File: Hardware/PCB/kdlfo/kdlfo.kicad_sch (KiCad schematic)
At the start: 51 parts, among them J1 Synth_power_2x5, J10 AudioJack2, J11 AudioJack2, J12 2 PIN MOLEX HEADER, J13 2 PIN MOLEX CONNECTOR, J2 2 PIN MOLEX HEADER, J3 2 PIN MOLEX HEADER, J4 AudioJack2, J5 2 PIN MOLEX HEADER, J6 2 PIN MOLEX CONNECTOR, J7 2 PIN MOLEX CONNECTOR, J8 2 PIN MOLEX CONNECTOR, J9 3 POSITION PIN HEADER, Q1 J201, Q2 J201, U1 TL074, U2 TL074

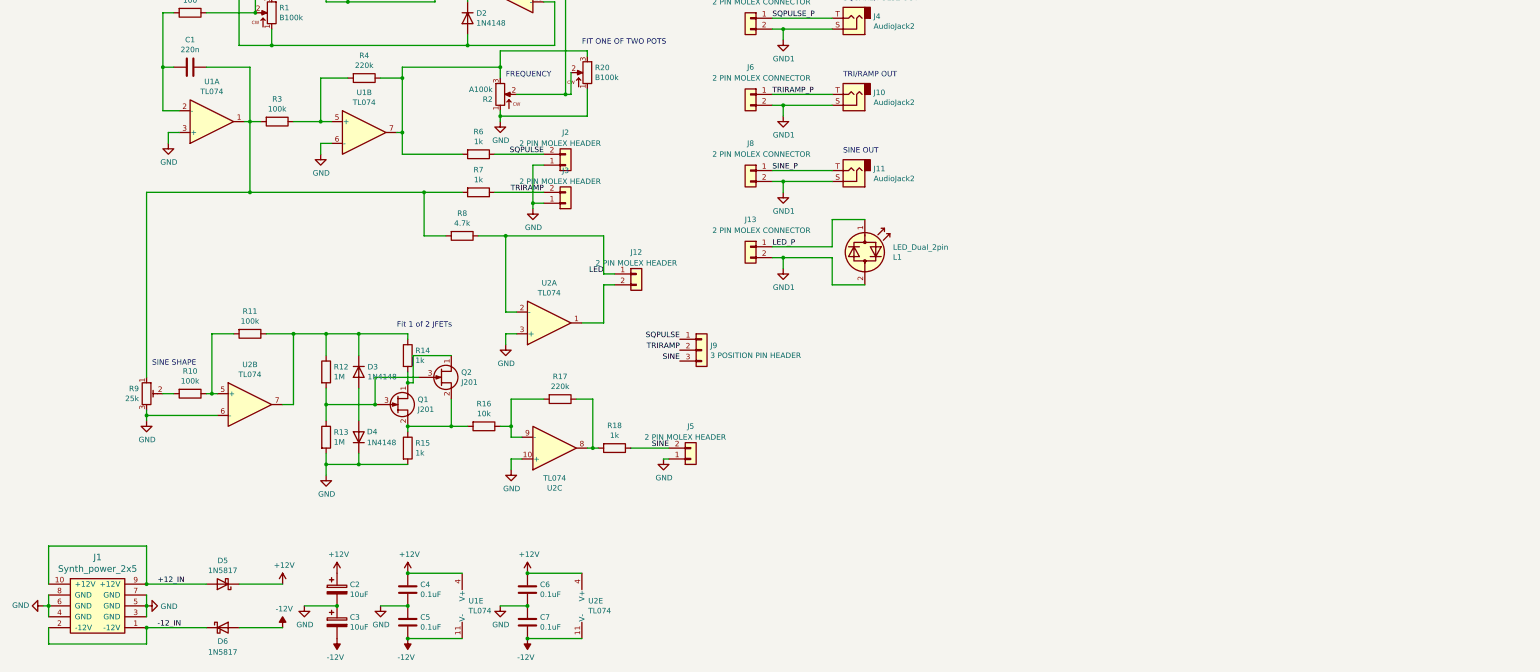
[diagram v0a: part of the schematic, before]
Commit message: Replace sine shaper, add divider on pulse output
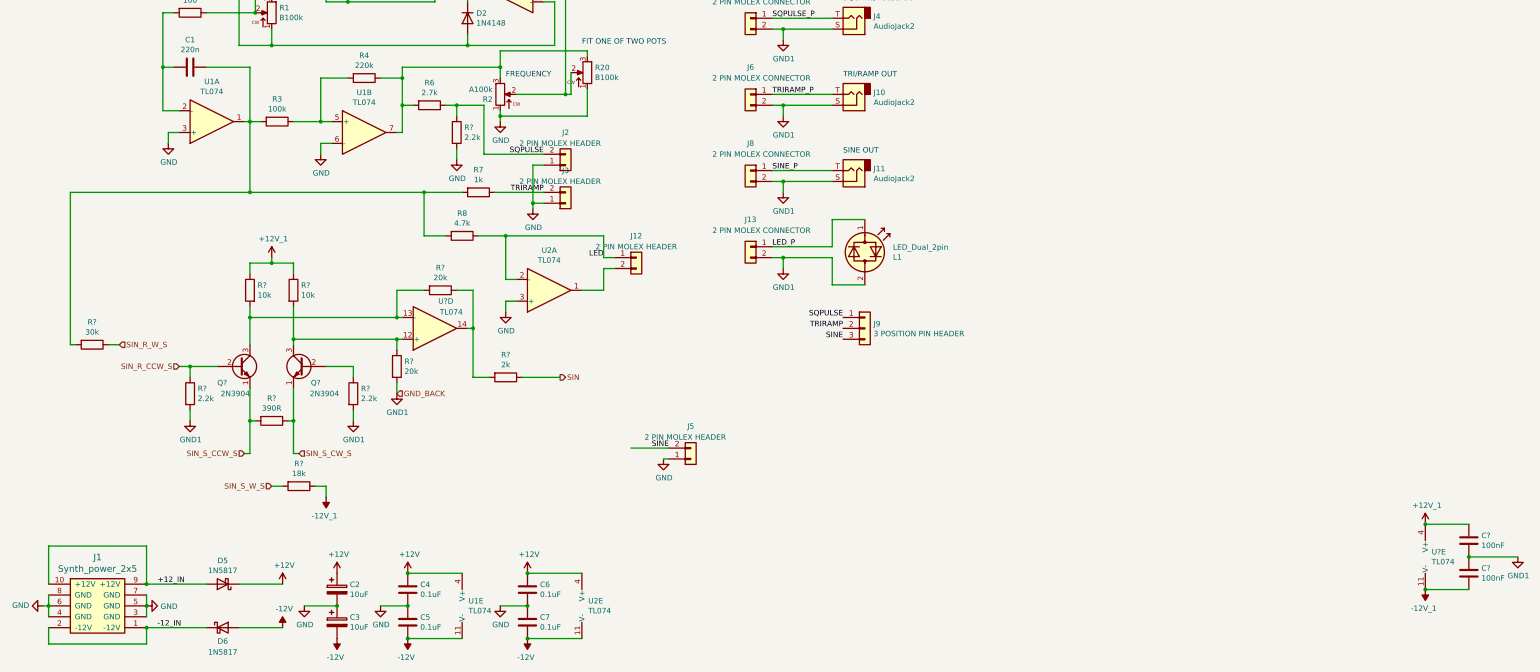
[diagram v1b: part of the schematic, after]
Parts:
- removed D3, D4: 1N4148, ao_tht:D_DO-35_SOD27_P7.62mm_Horizontal, symbol Diode:1N4148
- removed Q1: J201, ao_tht:TO-92_Inline_Wide, symbol Device:Q_NJFET_DSG
- removed Q2: J201, Package_TO_SOT_SMD:SOT-23, symbol Device:Q_NJFET_DSG
- removed R10, R11: 100k, ao_tht:R_Axial_DIN0207_L6.3mm_D2.5mm_P10.16mm_Horizontal, symbol Device:R
- removed R12, R13: 1M, ao_tht:R_Axial_DIN0207_L6.3mm_D2.5mm_P10.16mm_Horizontal, symbol Device:R
- removed R14, R15, R18: 1k, ao_tht:R_Axial_DIN0207_L6.3mm_D2.5mm_P10.16mm_Horizontal, symbol Device:R
- removed R16: 10k, ao_tht:R_Axial_DIN0207_L6.3mm_D2.5mm_P10.16mm_Horizontal, symbol Device:R
- removed R17: 220k, ao_tht:R_Axial_DIN0207_L6.3mm_D2.5mm_P10.16mm_Horizontal, symbol Device:R
- removed R9: 25k, ao_tht:Potentiometer_Bourns_3296W_Vertical, symbol Device:R_POT_TRIM
- removed unit 2 of U2
- removed unit 3 of U2
- added C? (x2): 100nF, ao_tht:C_Disc_D3.0mm_W1.6mm_P2.50mm, symbol ao_symbols:C
- added Q? (x2): 2N3904, ao_tht:TO-92_Inline_Wide, symbol ao_symbols:2N3904
- added R? (x2): 20k, ao_tht:R_Axial_DIN0207_L6.3mm_D2.5mm_P10.16mm_Horizontal, symbol ao_symbols:R
- added R? (x3): 2.2k, ao_tht:R_Axial_DIN0207_L6.3mm_D2.5mm_P10.16mm_Horizontal, symbol ao_symbols:R
- added R? (x2): 10k, ao_tht:R_Axial_DIN0207_L6.3mm_D2.5mm_P10.16mm_Horizontal, symbol ao_symbols:R
- added R?: 390R, ao_tht:R_Axial_DIN0207_L6.3mm_D2.5mm_P10.16mm_Horizontal, symbol ao_symbols:R
- added R?: 2k, ao_tht:R_Axial_DIN0207_L6.3mm_D2.5mm_P10.16mm_Horizontal, symbol ao_symbols:R
- added R?: 18k, ao_tht:R_Axial_DIN0207_L6.3mm_D2.5mm_P10.16mm_Horizontal, symbol ao_symbols:R
- added R?: 30k, ao_tht:R_Axial_DIN0207_L6.3mm_D2.5mm_P10.16mm_Horizontal, symbol ao_symbols:R
- added U? (x2): TL074, ao_tht:DIP-14_W7.62mm_Socket_LongPads, symbol Amplifier_Operational:TL074
- R6: value 1k -> 2.7k
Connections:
- net GND: now also R?.2
- net GND1: now also C?.1, C?.2, R?.2, R?.2, R?.2
- net SQPULSE: now also R?.1
- net at C1.1, R3.2, R7.2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: now also R?.2
- new net: R?.1, R?.2, U?.14
- new net: Q?.3 (C), R?.2, R?.2, U?.13 (-)
- new net: Q?.3 (C), R?.1, R?.2, U?.12 (+)
- new net: Q?.2 (B), R?.1
- new net +12V_1: C?.1, R?.1, R?.1, U?.4 (V+)
- new net -12V_1: C?.2, R?.1, U?.11 (V-)
- new net SIN: R?.1
- new net SIN_R_CCW_S: Q?.2 (B), R?.1
- new net SIN_R_W_S: R?.1
- new net SIN_S_CCW_S: Q?.1 (E), R?.2
- new net SIN_S_CW_S: Q?.1 (E), R?.1
- new net SIN_S_W_S: R?.2
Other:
- note removed: "Fit 1 of 2 JFETs"
- note removed: "SINE SHAPE"
- moved on the sheet: J12, J9, R6, U2A

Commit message: Better .gitignore; rm extraneous footprint library; misc revisions
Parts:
- removed J12, J2, J3, J5: 2 PIN MOLEX HEADER, ao_tht:Molex_KK-254_AE-6410-02A_1x02_P2.54mm_Vertical, symbol Connector_Generic:Conn_01x02
- removed J13, J6, J7, J8: 2 PIN MOLEX CONNECTOR, ao_tht:Molex_KK-254_AE-6410-02A_1x02_P2.54mm_Vertical, symbol Connector_Generic:Conn_01x02
- removed J9: 3 POSITION PIN HEADER, Connector_PinSocket_2.54mm:PinSocket_1x03_P2.54mm_Vertical, symbol Connector_Generic:Conn_01x03
- removed R19: B100k, ao_tht:Potentiometer_Alpha_RD901F-40-00D_Single_Vertical_CircularHoles, symbol ao_symbols:R_POT
- removed R2: A100k, Potentiometer_THT:Potentiometer_Piher_T-16H_Single_Horizontal, symbol ao_symbols:R_POT
- removed R?: 18k, ao_tht:R_Axial_DIN0207_L6.3mm_D2.5mm_P10.16mm_Horizontal, symbol ao_symbols:R
- added C1: 220n, ao_tht:C_Rect_L7.2mm_W2.5mm_P5.00mm_FKS2_FKP2_MKS2_MKP2, symbol Device:C
- added D1, D3: 1N4148, ao_tht:D_DO-35_SOD27_P7.62mm_Horizontal, symbol Diode:1N4148
- added D5: LED_Dual_2pin, ao_tht:LED_D5.0mm, symbol Device:LED_Dual_2pin
- added GRAF1: Holes, kdlfo:kdlfo_panel_holes, symbol ao_symbols:Graphic
- added J1, J3, J5, J7: 3_pin_Molex_header, ao_tht:Molex_KK-254_AE-6410-03A_1x03_P2.54mm_Vertical, symbol ao_symbols:3_pin_Molex_header
- added J11, J13, J9: AudioJack2, ao_tht:Jack_6.35mm_PJ_629HAN, symbol Connector:AudioJack2
- added J2, J4, J6, J8: 3_pin_Molex_connector, symbol ao_symbols:3_pin_Molex_connector
- added Q1, Q2: 2N3904, ao_tht:TO-92_Inline_Wide, symbol ao_symbols:2N3904
- added R1: 100, ao_tht:R_Axial_DIN0207_L6.3mm_D2.5mm_P10.16mm_Horizontal, symbol Device:R
- added R11: 1k, ao_tht:R_Axial_DIN0207_L6.3mm_D2.5mm_P10.16mm_Horizontal, symbol Device:R
- added R13: 4.7k, ao_tht:R_Axial_DIN0207_L6.3mm_D2.5mm_P10.16mm_Horizontal, symbol Device:R
- added R15, R16: 10k, ao_tht:R_Axial_DIN0207_L6.3mm_D2.5mm_P10.16mm_Horizontal, symbol ao_symbols:R
- added R17, R23: 20k, ao_tht:R_Axial_DIN0207_L6.3mm_D2.5mm_P10.16mm_Horizontal, symbol ao_symbols:R
- added R21: 47k, ao_tht:R_Axial_DIN0207_L6.3mm_D2.5mm_P10.16mm_Horizontal, symbol ao_symbols:R
- added R24: 2k, ao_tht:R_Axial_DIN0207_L6.3mm_D2.5mm_P10.16mm_Horizontal, symbol ao_symbols:R
- added R27, R28, R8: 2.2k, ao_tht:R_Axial_DIN0207_L6.3mm_D2.5mm_P10.16mm_Horizontal, symbol ao_symbols:R
- added R3: 220k, ao_tht:R_Axial_DIN0207_L6.3mm_D2.5mm_P10.16mm_Horizontal, symbol Device:R
- added R31: 390R, ao_tht:R_Axial_DIN0207_L6.3mm_D2.5mm_P10.16mm_Horizontal, symbol ao_symbols:R
- added R33, R34: 18k, ao_tht:R_Axial_DIN0207_L6.3mm_D2.5mm_P10.16mm_Horizontal, symbol ao_symbols:R
- added R5: 2.7k, ao_tht:R_Axial_DIN0207_L6.3mm_D2.5mm_P10.16mm_Horizontal, symbol Device:R
- added R7: 100k, ao_tht:R_Axial_DIN0207_L6.3mm_D2.5mm_P10.16mm_Horizontal, symbol Device:R
- added RV1, RV3: B100k, ao_tht:Potentiometer_Alpha_16mm_Single_Vertical, symbol ao_symbols:R_POT
- added RV10, RV9: B50k, ao_tht:Potentiometer_Bourns_3296W_Vertical_standard, symbol ao_symbols:R_POT_TRIM_3296W
- added RV5, RV6: B50K, ao_tht:Potentiometer_Bourns_3296W_Vertical_standard, symbol ao_symbols:R_POT_TRIM_3296W
- added RV7, RV8: B5K, ao_tht:Potentiometer_Bourns_3296W_Vertical_standard, symbol ao_symbols:R_POT_TRIM_3296W
- added TP1: -12V, ao_tht:TestPoint_THTPad_D1.5mm_Drill0.7mm, symbol ao_symbols:TestPoint
- added TP2: +12V, ao_tht:TestPoint_THTPad_D1.5mm_Drill0.7mm, symbol ao_symbols:TestPoint
- added TP3: GND, ao_tht:TestPoint_THTPad_1.5x1.5mm_Drill0.7mm, symbol ao_symbols:TestPoint
- added unit 3 of U1
- added unit 4 of U1
- added unit 4 of U2
- added unit 3 of U2
- added unit 3 of U3
- added unit 4 of U3
- R22: renamed from R?; value 30k -> 47k
- RV2: renamed from R1; footprint Potentiometer_THT:Potentiometer_Piher_T-16H_Single_Horizontal -> ao_tht:Potentiometer_Alpha_16mm_Single_Vertical
- RV4: renamed from R20; footprint ao_tht:Potentiometer_Alpha_RD901F-40-00D_Single_Vertical_CircularHoles -> ao_tht:Potentiometer_Alpha_16mm_Single_Vertical
- gave numbers to parts that had none: 14
- renumbered C1 to C2, C2 to C3, C6 to C5, C3 to C7, C5 to C8, C7 to C9, D1 to D2, D2 to D4, L1 to D6, D5 to D7, D6 to D8, J4 to J10, J10 to J12, J11 to J14, J1 to J15, R7 to R12, R8 to R14, R5 to R2, R3 to R9, U1 to U2, U2 to U3
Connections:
- net +12V_1 is gone; now on net +12V: C6.1, R18.1, R19.1, U3.4 (V+)
- net -12V_1 is gone; now on net -12V: C10.2, U3.11 (V-)
- net LED_P is gone; now on an unnamed net: D6.1 (KA)
- net SINE_P is gone; now on net SINE_A: J14.T
- net +12V: now also R15.1, R16.1, TP2.1
- net -12V: now also R33.1, R34.1, TP1.1
- net GND: now also C10.1, C6.2, J10.S, J12.S, J14.S, R25.2, R29.2, R30.2, U3.5 (+), J11.S, J13.S, J5.1 (Pin_1), J7.1 (Pin_1), J9.S, R23.2, R27.2, R28.2, R8.2, RV7.2, RV7.3, RV8.2, RV8.3, TP3.1, U2.12 (+), U2.9 (-), U3.10 (+); no longer RV4.1, U3.3 (+)
- net SINE: now also J13.T, R24.1, RV7.1
- net SQPULSE: now also J9.T, R5.1, R8.1; no longer R10.1, R6.1
- net TRIRAMP: now also J11.T, R11.1; no longer R12.1
- net FRPOTCW_A: now reaches R4.1, R6.2, U2.7
- net FRPOTCW_A: now also J7.3 (Pin_3); no longer RV4.3
- net at D2.2 (A): now also U1.1; no longer U1.8
- net at D4.1 (K): now also U1.7; no longer U1.14
- net at RV2.2: now also J4.2 (Pin_2); no longer R2.1
- net at R20.1, R26.2: now also U3.1; no longer U3.14
- net at Q3.3 (C), R18.2, R20.2: now also U3.2 (-); no longer U3.13 (-)
- net at Q4.3 (C), R19.2, R25.1: now also U3.3 (+); no longer U3.12 (+)
- removed net GND1: C10.1, C6.2, D6.2 (AK), J10.S, J12.S, J14.S, R25.2, R29.2, R30.2
- net LED: no longer names the net of R14.1
- net LED: now also U3.6 (-); no longer U3.2 (-)
- net SIN renamed SINE_A
- net SINE_A: now also RV8.1
- net SIN_R_CCW_S: no longer names the net of Q3.2 (B), R29.1
- net SIN_R_CCW_S: now also RV6.3
- net SIN_R_W_S renamed SINE_ROUND_A
- net SINE_ROUND_A: now also RV6.1, RV6.2
- net SIN_S_CCW_S: no longer names the net of Q3.1 (E), R32.2
- net SIN_S_CCW_S: now also RV10.1
- net SIN_S_CW_S: no longer names the net of Q4.1 (E), R32.1
- net SIN_S_CW_S: now also RV10.3
- net SQPULSE_P renamed SQPULSE_A
- net SQPULSE_A: now also R10.1, R6.1
- net TRIRAMP_P renamed TRIRAMP_A
- net TRIRAMP_A: now also R12.1
- new net: J4.1 (Pin_1), RV2.1
- new net: J4.3 (Pin_3), RV2.3
- new net: D6.2 (AK), U3.7
- new net: J8.1 (Pin_1), RV4.1
- new net: J8.2 (Pin_2), RV4.2
- new net: J8.3 (Pin_3), RV4.3
- new net: D3.1 (K), U1.8
- new net: J6.1 (Pin_1), RV3.1
- new net: J6.2 (Pin_2), RV3.2
- new net: J6.3 (Pin_3), RV3.3
- new net: D5.1 (KA), R13.1, U3.9 (-)
- new net: D5.2 (AK), U3.8
- new net: C1.2, R1.2, U2.13 (-)
- new net: R3.2, R7.1, U2.10 (+)
- new net: C1.1, R11.2, R13.2, R21.2, R7.2, U2.14
- new net: Q2.1 (E), R31.1, RV9.3
- new net: Q2.2 (B), R28.1
- new net: Q2.3 (C), R16.2, R23.1, U3.12 (+)
- new net: Q1.1 (E), R31.2, RV9.1
- new net: Q1.2 (B), R27.1, RV5.3
- new net: Q1.3 (C), R15.2, R17.2, U3.13 (-)
- new net: D1.2 (A), U1.14
- new net: R17.1, R24.2, U3.14
- new net: J2.1 (Pin_1), RV1.1
- new net: J2.2 (Pin_2), RV1.2
- new net: J2.3 (Pin_3), RV1.3
- new net FRPOTCW: J5.3 (Pin_3), R3.1, R5.2, U2.8
- new net FRPOTW: J5.2 (Pin_2), U1.10 (+), U1.12 (+)
- new net FRPOTW_A: J7.2 (Pin_2), U1.3 (+), U1.5 (+)
- new net SHPOTCCW: D3.2 (A), J1.1 (Pin_1), U1.9 (-)
- new net SHPOTCCW_A: D4.2 (A), J3.1 (Pin_1), U1.6 (-)
- new net SHPOTCW: D1.1 (K), J1.3 (Pin_3), U1.13 (-)
- new net SHPOTCW_A: D2.1 (K), J3.3 (Pin_3), U1.2 (-)
- new net SHPOTW: J1.2 (Pin_2), R1.1
- new net SHPOTW_A: J3.2 (Pin_2), R2.1
- new net SINE_ROUND: R21.1, RV5.1, RV5.2
- new net SINE_SYM: R33.2, RV9.2
- new net SINE_SYM_A: R34.2, RV10.2
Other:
- note added: "Add switched capacitor?"
- note removed: "SINE OUT"
- note removed: "SQUARE/PULSE OUT"
- note removed: "TRI/RAMP OUT"
- moved on the sheet: C10, C6, D6, J10, J12, J14, RV2, RV4, U3B, U3E

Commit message: Reorg schematic, redo layout
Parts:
- removed C1, C2: 220n, ao_tht:C_Rect_L7.2mm_W2.5mm_P5.00mm_FKS2_FKP2_MKS2_MKP2, symbol Device:C
- removed C10, C6: 100nF, ao_tht:C_Disc_D3.0mm_W1.6mm_P2.50mm, symbol ao_symbols:C
- removed C4, C5, C8, C9: 0.1uF, ao_tht:C_Disc_D3.0mm_W1.6mm_P2.50mm, symbol Device:C
- removed D1, D2, D3, D4: 1N4148, ao_tht:D_DO-35_SOD27_P7.62mm_Horizontal, symbol Diode:1N4148
- removed D5, D6: LED_Dual_2pin, ao_tht:LED_D5.0mm, symbol Device:LED_Dual_2pin
- removed J10, J11, J12, J13, J14, J9: AudioJack2, ao_tht:Jack_6.35mm_PJ_629HAN, symbol Connector:AudioJack2
- removed J2: 3_pin_Molex_connector, symbol ao_symbols:3_pin_Molex_connector
- removed J5: 3_pin_Molex_header, ao_tht:Molex_KK-254_AE-6410-03A_1x03_P2.54mm_Vertical, symbol ao_symbols:3_pin_Molex_header
- removed Q1, Q2, Q3, Q4: 2N3904, ao_tht:TO-92_Inline_Wide, symbol ao_symbols:2N3904
- removed R1, R2: 100, ao_tht:R_Axial_DIN0207_L6.3mm_D2.5mm_P10.16mm_Horizontal, symbol Device:R
- removed R10, R27, R28, R29, R30, R8: 2.2k, ao_tht:R_Axial_DIN0207_L6.3mm_D2.5mm_P10.16mm_Horizontal, symbol ao_symbols:R
- removed R11, R12: 1k, ao_tht:R_Axial_DIN0207_L6.3mm_D2.5mm_P10.16mm_Horizontal, symbol Device:R
- removed R13, R14: 4.7k, ao_tht:R_Axial_DIN0207_L6.3mm_D2.5mm_P10.16mm_Horizontal, symbol Device:R
- removed R15, R16, R18, R19: 10k, ao_tht:R_Axial_DIN0207_L6.3mm_D2.5mm_P10.16mm_Horizontal, symbol ao_symbols:R
- removed R17, R20, R23, R25: 20k, ao_tht:R_Axial_DIN0207_L6.3mm_D2.5mm_P10.16mm_Horizontal, symbol ao_symbols:R
- removed R21, R22: 47k, ao_tht:R_Axial_DIN0207_L6.3mm_D2.5mm_P10.16mm_Horizontal, symbol ao_symbols:R
- removed R24, R26: 2k, ao_tht:R_Axial_DIN0207_L6.3mm_D2.5mm_P10.16mm_Horizontal, symbol ao_symbols:R
- removed R3, R4: 220k, ao_tht:R_Axial_DIN0207_L6.3mm_D2.5mm_P10.16mm_Horizontal, symbol Device:R
- removed R31, R32: 390R, ao_tht:R_Axial_DIN0207_L6.3mm_D2.5mm_P10.16mm_Horizontal, symbol ao_symbols:R
- removed R33, R34: 18k, ao_tht:R_Axial_DIN0207_L6.3mm_D2.5mm_P10.16mm_Horizontal, symbol ao_symbols:R
- removed R5, R6: 2.7k, ao_tht:R_Axial_DIN0207_L6.3mm_D2.5mm_P10.16mm_Horizontal, symbol Device:R
- removed R7, R9: 100k, ao_tht:R_Axial_DIN0207_L6.3mm_D2.5mm_P10.16mm_Horizontal, symbol Device:R
- removed RV10, RV9: B50k, ao_tht:Potentiometer_Bourns_3296W_Vertical_standard, symbol ao_symbols:R_POT_TRIM_3296W
- removed RV5, RV6: B50K, ao_tht:Potentiometer_Bourns_3296W_Vertical_standard, symbol ao_symbols:R_POT_TRIM_3296W
- removed RV7, RV8: B5K, ao_tht:Potentiometer_Bourns_3296W_Vertical_standard, symbol ao_symbols:R_POT_TRIM_3296W
- removed U1, U2, U3: TL074, ao_tht:DIP-14_W7.62mm_Socket_LongPads, symbol Amplifier_Operational:TL074
- added J2: 3_pin_Molex_header, ao_tht:Molex_KK-254_AE-6410-03A_1x03_P2.54mm_Vertical, symbol ao_symbols:3_pin_Molex_header
- added J5: 3_pin_Molex_connector, ao_tht:Molex_KK-254_AE-6410-03A_1x03_P2.54mm_Vertical, symbol ao_symbols:3_pin_Molex_connector
- C3: footprint ao_tht:CP_Radial_D5.0mm_P2.00mm -> ao_tht:CP_Radial_D6.3mm_P2.50mm; symbol Device:CP -> ao_symbols:CP; Vendor (none) -> Tayda
- C7: value 10uF -> (none); footprint ao_tht:CP_Radial_D5.0mm_P2.00mm -> ao_tht:CP_Radial_D6.3mm_P2.50mm; symbol Device:CP -> ao_symbols:CP; Vendor (none) -> Tayda
- J15: SKU (none) -> A-2939; Vendor (none) -> Tayda
- J4, J8: value 3_pin_Molex_connector -> (none); footprint (none) -> ao_tht:Molex_KK-254_AE-6410-03A_1x03_P2.54mm_Vertical
- J6: footprint (none) -> ao_tht:Molex_KK-254_AE-6410-03A_1x03_P2.54mm_Vertical
- RV2, RV4: value B100k -> (none); footprint ao_tht:Potentiometer_Alpha_16mm_Single_Vertical -> (none)
- TP1, TP2: Config (none) -> DNF
- TP3: footprint ao_tht:TestPoint_THTPad_1.5x1.5mm_Drill0.7mm -> ao_tht:TestPoint_THTPad_D1.5mm_Drill0.7mm; Config (none) -> DNF
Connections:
- net GND: now also J2.1 (Pin_1)
- net at RV1.1: now also J5.1 (Pin_1)
- net at RV1.2: now also J5.2 (Pin_2)
- net at RV1.3: now also J5.3 (Pin_3)
- net FRPOTCW_A renamed LFO A/FRPOTW
- net FRPOTW_A renamed LFO A/FRPOTCW
- net SHPOTCCW renamed LFO B/SHPOTCW
- net SHPOTCCW_A renamed LFO A/SHPOTCW
- net SHPOTCW renamed LFO B/SHPOTCCW
- net SHPOTCW_A renamed LFO A/SHPOTCCW
- net SHPOTW renamed LFO B/SHPOTW
- net SHPOTW_A renamed LFO A/SHPOTW
- new net LFO B/FRPOTCW: J2.2 (Pin_2)
- new net LFO B/FRPOTW: J2.3 (Pin_3)
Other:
- added sheet LFO A (onelfo.kicad_sch)
- added sheet LFO B (onelfo.kicad_sch)
- note added: "FREQUENCY A"
- note added: "SHAPE A"
- note removed: "Add switched capacitor?"
- note removed: "FIT ONE OF TWO POTS"
- note removed: "FREQUENCY"
- note removed: "SHAPE"
- moved on the sheet: C3, C7, D7, D8, J15, J3, J4, J7, J8, RV2, RV4, TP1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
